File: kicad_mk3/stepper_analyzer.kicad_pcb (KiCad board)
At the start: 2 copper layers, 102 x 57 mm, 22 parts, among them J1 Connector_Conn_01x04_Male, J2 Connector_Conn_01x04_Male, M1 Motor, Q1 AO3400A, U1 ACS70331EOLCTR-2P5B3, U2 ACS70331EOLCTR-2P5B3, U3 Pico

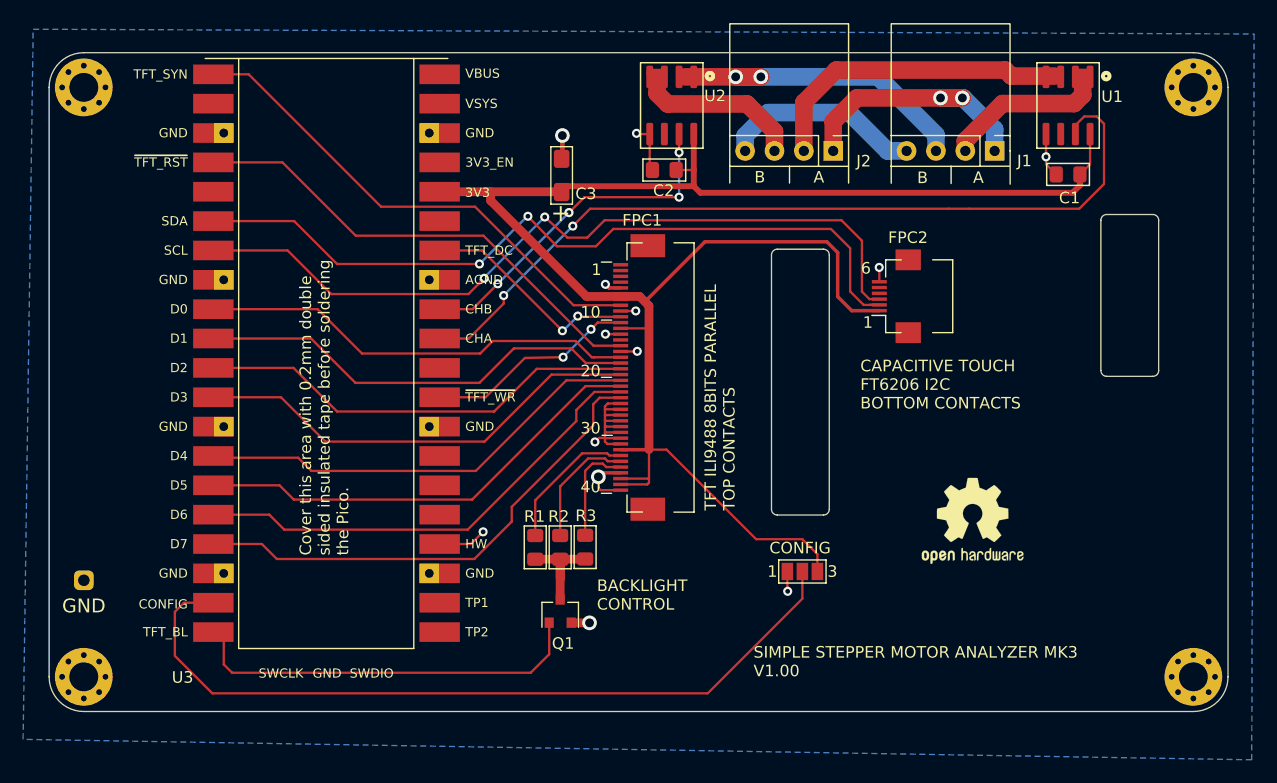
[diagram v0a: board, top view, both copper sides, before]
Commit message: Tweaked TFT insulation.
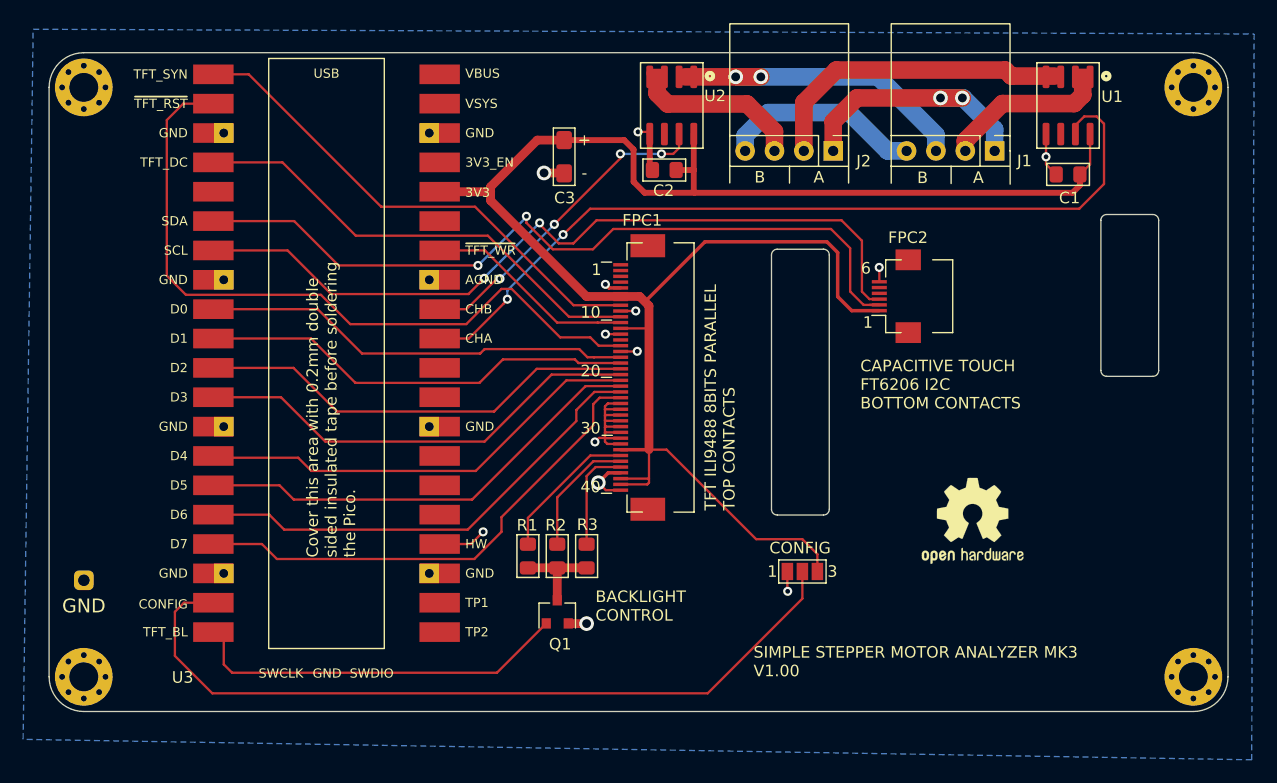
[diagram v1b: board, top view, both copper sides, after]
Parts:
- moved C3 1.63 mm to (43.6, -48.0), turned to 270 degrees
- moved R1 0.99 mm to (40.4, -13.4)
- moved R2 0.79 mm to (43.0, -13.4)
- moved R3 0.78 mm to (45.5, -13.4)
- moved Q1 0.26 mm to (43.0, -8.62)
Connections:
- U3 pad 2: Net-(U3-Pad2) -> /~TFT_RST
- U3 pad 29: /~TFT_WR -> Net-(U3-Pad29)
- U3 pad 34: /TFT_DC -> /~TFT_WR
- U3 pad 4: /~TFT_RST -> /TFT_DC
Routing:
- net /~TFT_RST: track 40.9 -> 63.3 mm
- net /TFT_DC: track 20.0 -> 39.9 mm, vias 2 -> 0
- net +3V3: track 158.6 -> 164.2 mm
- net /CHB: track 31.1 -> 28.8 mm
- net /TFT_BL: track 35.3 -> 33.5 mm
- net Net-(Q1-Pad3): track 9.48 -> 7.90 mm
- net GND: track 46.6 -> 45.3 mm
- net /D1: track 37.7 -> 36.9 mm
- net /SDA: track 67.5 -> 68.1 mm
- net /D0: track 37.0 -> 36.4 mm
- net /~TFT_WR: track 19.6 -> 19.1 mm, vias 2 -> 0
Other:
- board text added: "+"
- board text added: "-"
- board text added: "15x10mm"
- board text added: "75x10mm"
- board text added: "86x10mm"
- board text added: "The entire TFT area must be perfectly flat. Cut connector pins using the 3D model jig BEFORE inserting them. Attach the TFT with 0.2mm double sided insulated tape at the marked areas."
- board text removed: "The entire TFT area must be perfectly flat. Cut connector pins BEFORE inserting them. Attach the TFT with 0.2mm double sided insulated tape"

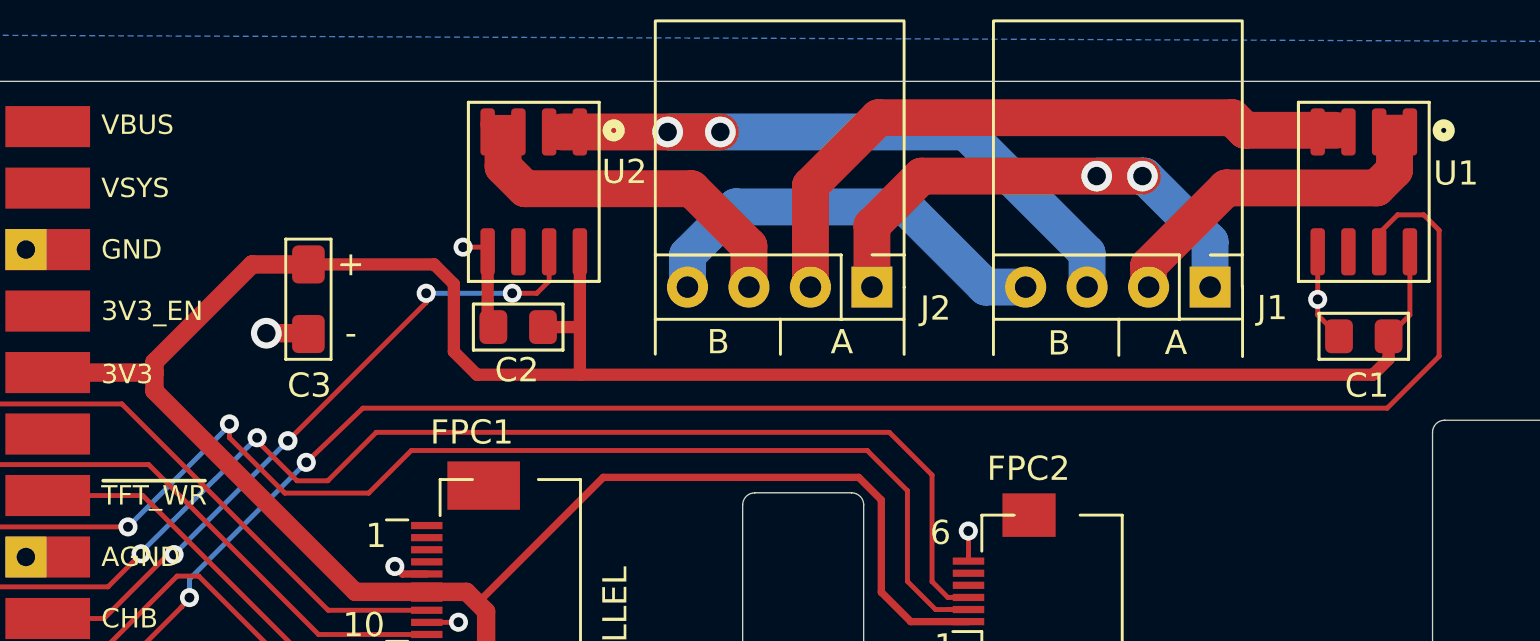
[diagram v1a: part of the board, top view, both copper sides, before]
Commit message: Cleaned up the +3.3V path.
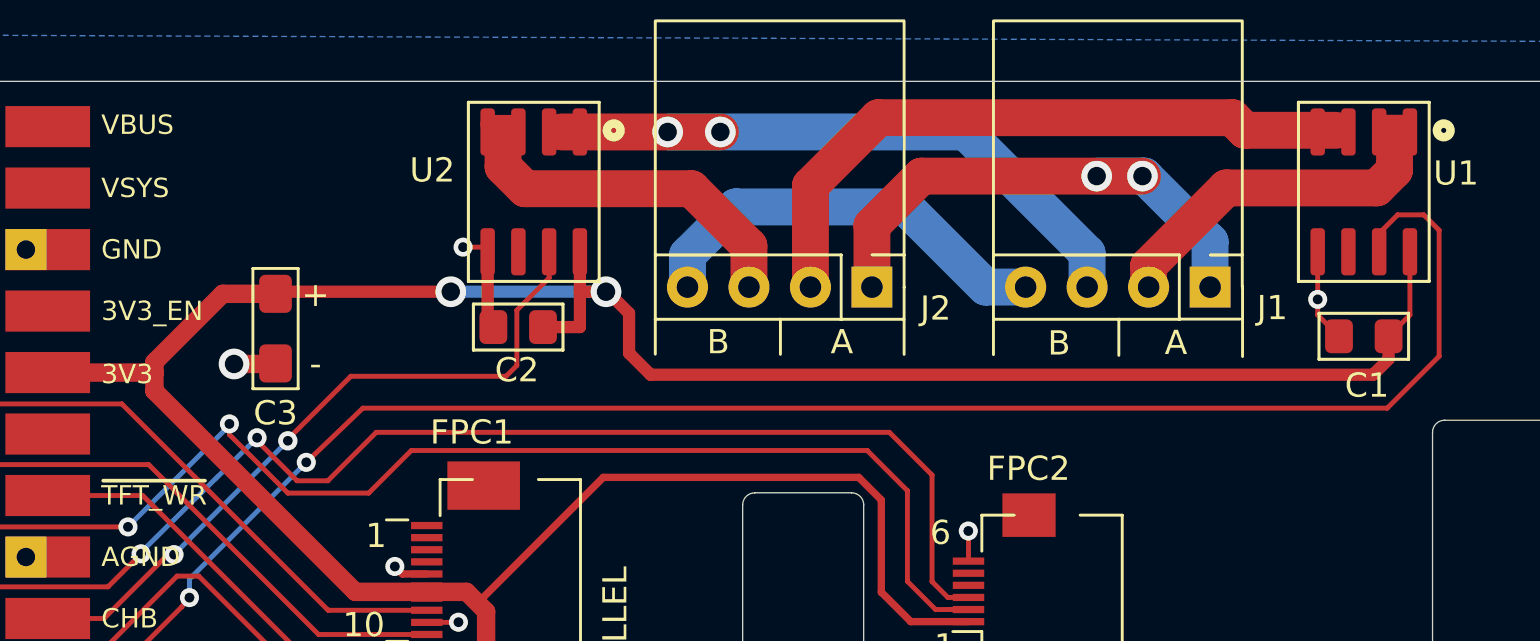
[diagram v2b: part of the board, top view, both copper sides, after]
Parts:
- moved C3 1.82 mm to (42.2, -46.8)
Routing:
- net +3V3: track 164.2 -> 161.8 mm, vias 0 -> 2
- net /CHB: track 28.8 -> 29.9 mm, vias 4 -> 2
